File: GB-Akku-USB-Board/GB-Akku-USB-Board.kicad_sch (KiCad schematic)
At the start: 18 parts, among them J1 USB_C_Receptacle_PowerOnly_6P, J2 Conn_01x01_Pin, J3 Conn_01x01_Pin, J4 Conn_01x01_Pin, J5 Conn_01x01_Pin, J6 Conn_01x01_Pin, J7 Conn_01x01_Pin, SW1 SW_Push

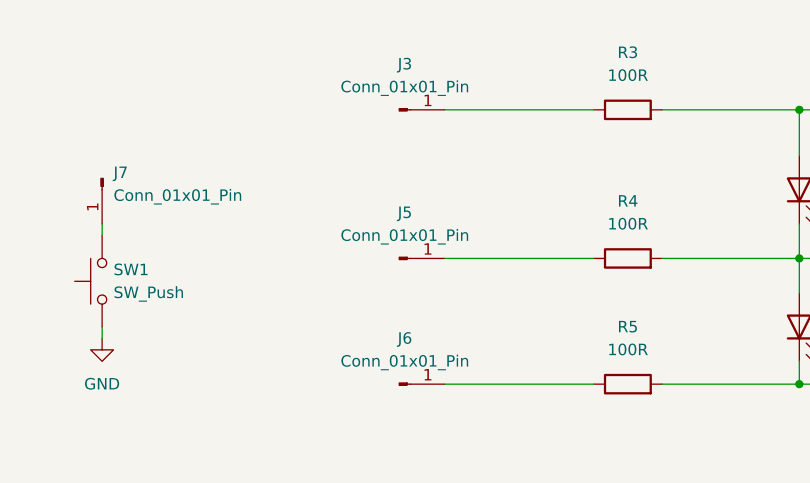
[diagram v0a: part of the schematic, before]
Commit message: STM32 BOOT0 Pin fixed
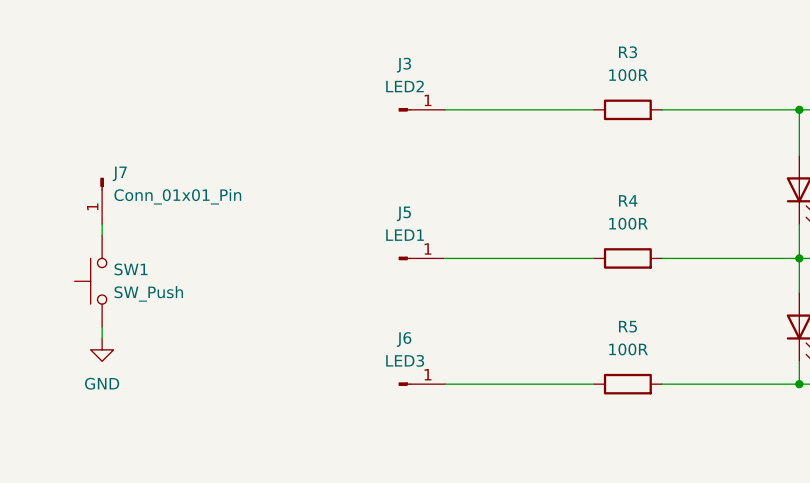
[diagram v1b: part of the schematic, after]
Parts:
- J3: value Conn_01x01_Pin -> LED2
- J5: value Conn_01x01_Pin -> LED1
- J6: value Conn_01x01_Pin -> LED3
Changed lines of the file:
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@@
 			)
 		)
-		(property "Value" "Conn_01x01_Pin"
+		(property "Value" "LED2"
 			(at 147.955 22.86 0)
 			(effects
@@
 			)
 		)
-		(property "Value" "Conn_01x01_Pin"
+		(property "Value" "LED3"
 			(at 147.955 53.34 0)
 			(effects
@@
 			)
 		)
-		(property "Value" "Conn_01x01_Pin"
+		(property "Value" "LED1"
 			(at 147.955 39.37 0)
 			(effects
